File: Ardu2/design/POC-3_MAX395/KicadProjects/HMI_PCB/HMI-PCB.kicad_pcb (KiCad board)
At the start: 2 copper layers, 170.2 x 75.2 mm, 41 parts, among them P1 SplitPot_0_M, P10 TREM_VIB, P11 SplitPot_5_TR, P12 Analog Power IN, P13 Digital Power IN/OUT, P2 SEQ_SAVE, P3 SplitPot_1_A, P4 SplitPot_2_B, P5 PB_OUT, P6 Analog_Out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

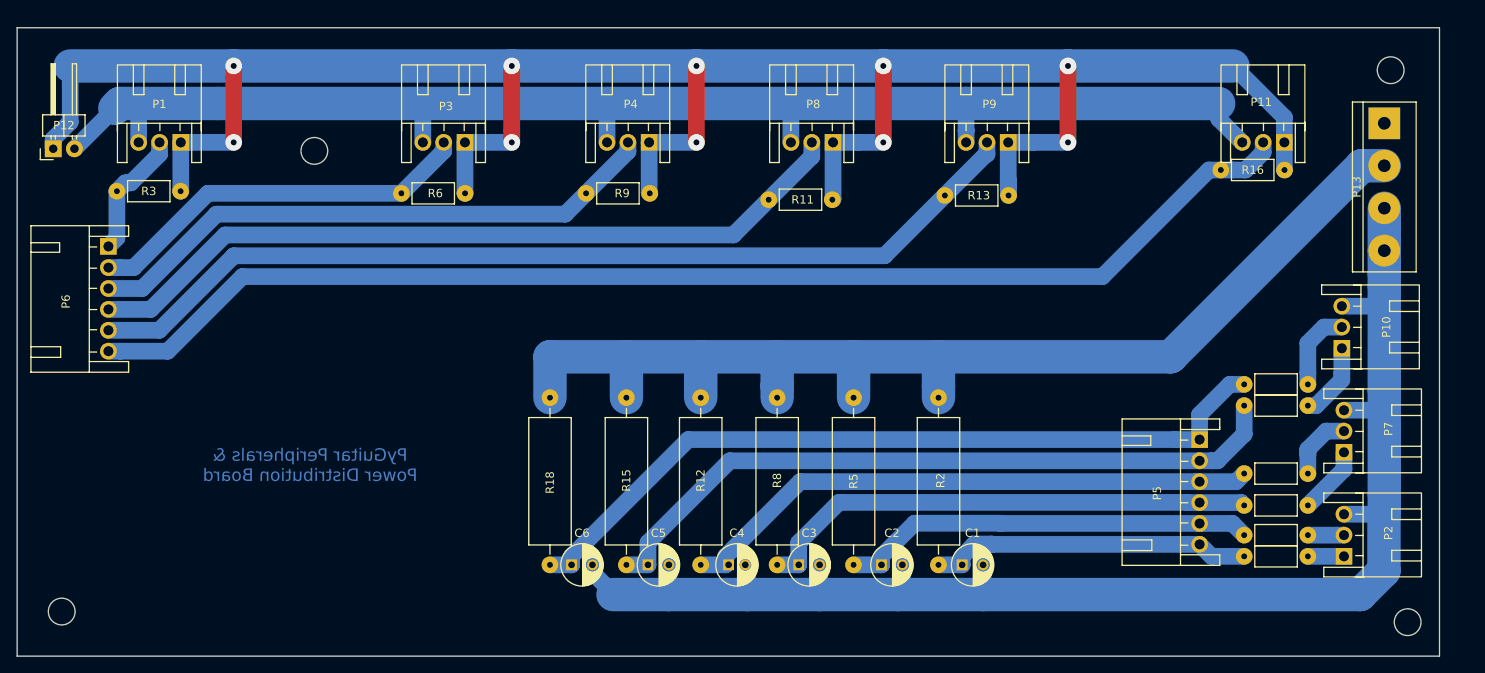
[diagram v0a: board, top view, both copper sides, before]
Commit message: updated peripherals PCB
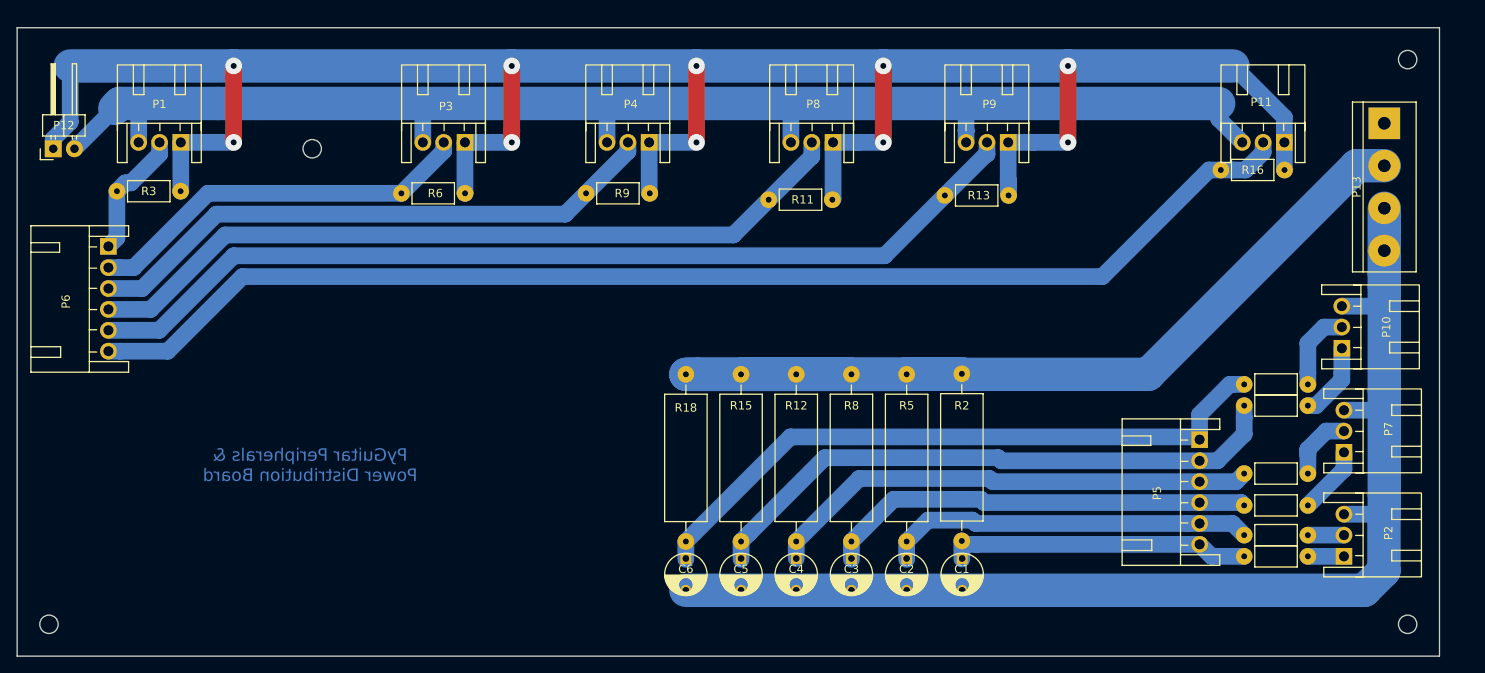
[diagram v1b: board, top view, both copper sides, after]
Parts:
- removed the REF** at (102.1, 86.9)
- removed the REF** at (232.9, 143.3)
- removed the REF** at (71.9, 142.0)
- removed the REF** at (230.9, 77.2)
- added REF**: MountingHole_2.2mm_M2, Mounting_Holes:MountingHole_2.2mm_M2, F.Cu at (70.4, 143.5)
- added REF**: MountingHole_2.2mm_M2, Mounting_Holes:MountingHole_2.2mm_M2, F.Cu at (101.9, 86.6)
- added REF**: MountingHole_2.2mm_M2, Mounting_Holes:MountingHole_2.2mm_M2, F.Cu at (232.9, 143.5)
- added REF**: MountingHole_2.2mm_M2, Mounting_Holes:MountingHole_2.2mm_M2, F.Cu at (232.9, 75.9)
- C1, C2, C3, C5, C6: footprint Capacitors_ThroughHole:C_Radial_D5_L11_P2.5 -> misc:C_Radial_D5_L11_P3.81
- C4: footprint Capacitors_ThroughHole:C_Radial_D5_L11_P2 -> misc:C_Radial_D5_L11_P3.81
- moved R18 16.5 mm to (146.6, 113.6)
- moved R15 14.0 mm to (153.2, 113.6)
- moved C6 13.7 mm to (146.6, 136.3), turned to 270 degrees
- moved R12 11.8 mm to (159.8, 113.6)
- moved C5 11.1 mm to (153.2, 136.3), turned to 270 degrees
- moved R8 9.32 mm to (166.4, 113.6)
- moved C4 8.10 mm to (159.8, 136.3), turned to 270 degrees
- moved R5 6.94 mm to (173.0, 113.6)
- moved C3 6.31 mm to (166.4, 136.3), turned to 270 degrees
- moved R2 4.00 mm to (179.6, 113.5)
- moved C2 3.01 mm to (173.0, 136.3), turned to 270 degrees
- moved C1 0.10 mm to (179.6, 136.3), turned to 270 degrees
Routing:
- net /GND_D: track 174.2 -> 142.7 mm
- net /X22: track 94.4 -> 78.8 mm
- net /X7: track 85.4 -> 71.4 mm
- net /Y6: track 70.2 -> 59.3 mm
- net /Y5: track 60.7 -> 51.5 mm
- net /Y4: track 50.0 -> 44.3 mm
- net /Y3: track 38.8 -> 36.7 mm
- net /3v3_D: track 138.6 -> 140.2 mm

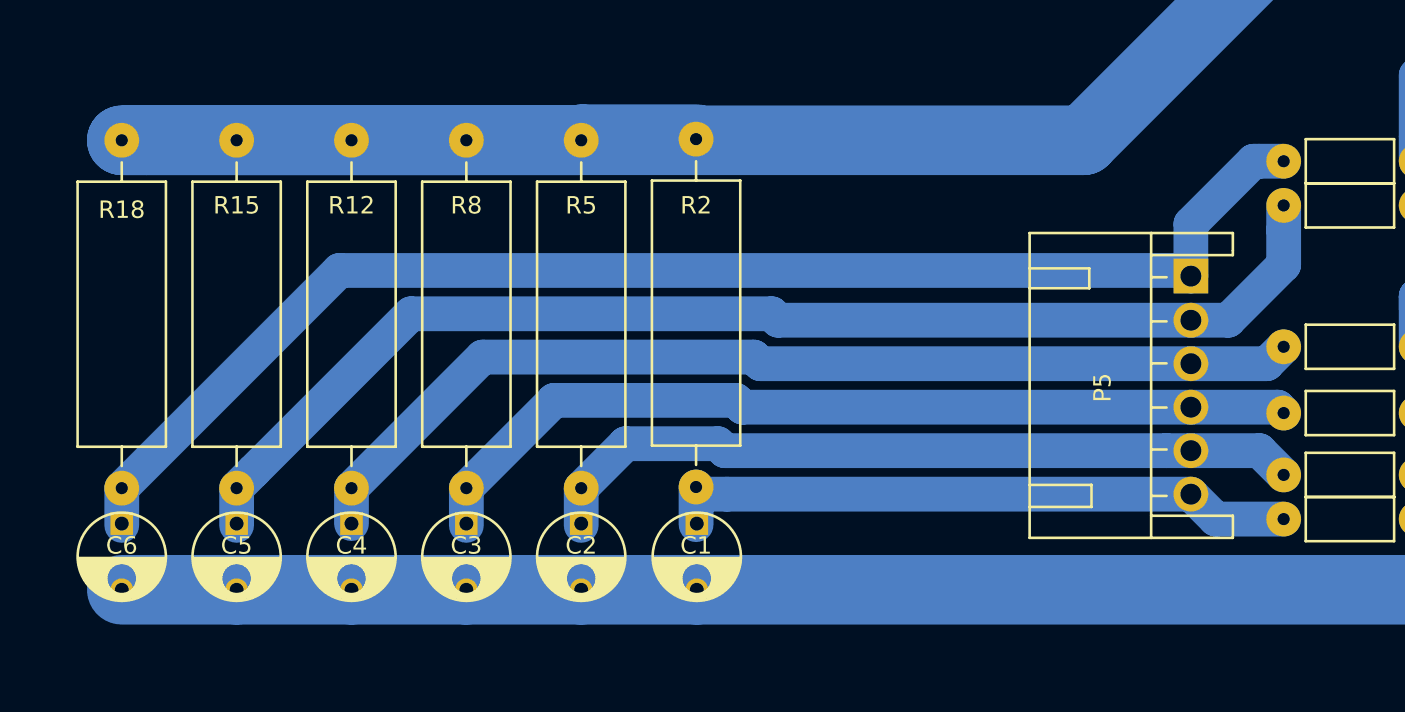
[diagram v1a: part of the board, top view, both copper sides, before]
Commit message: updated peripherals PCB
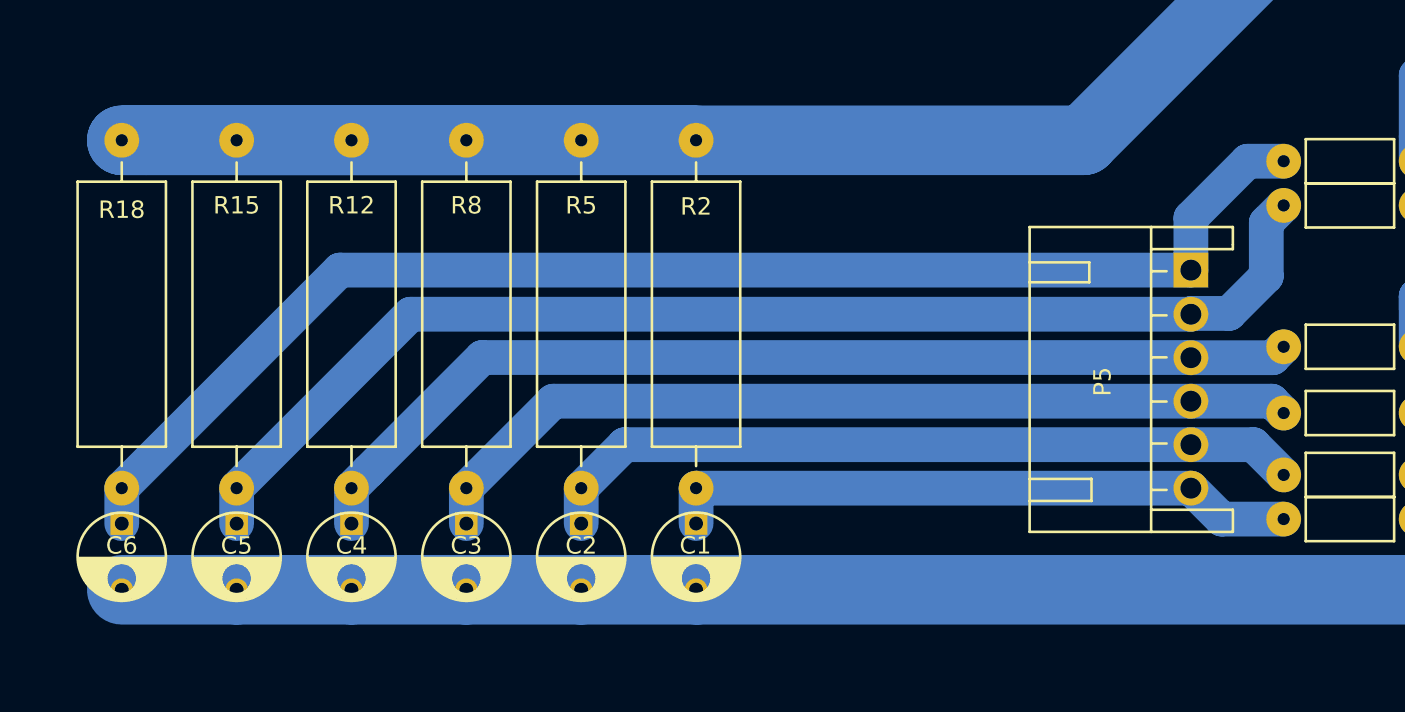
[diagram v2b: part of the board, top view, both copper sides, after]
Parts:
- moved P5 0.34 mm to (208.0, 121.1)
- moved R2 0.07 mm to (179.6, 113.6)
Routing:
- net /X7: track 71.4 -> 70.8 mm

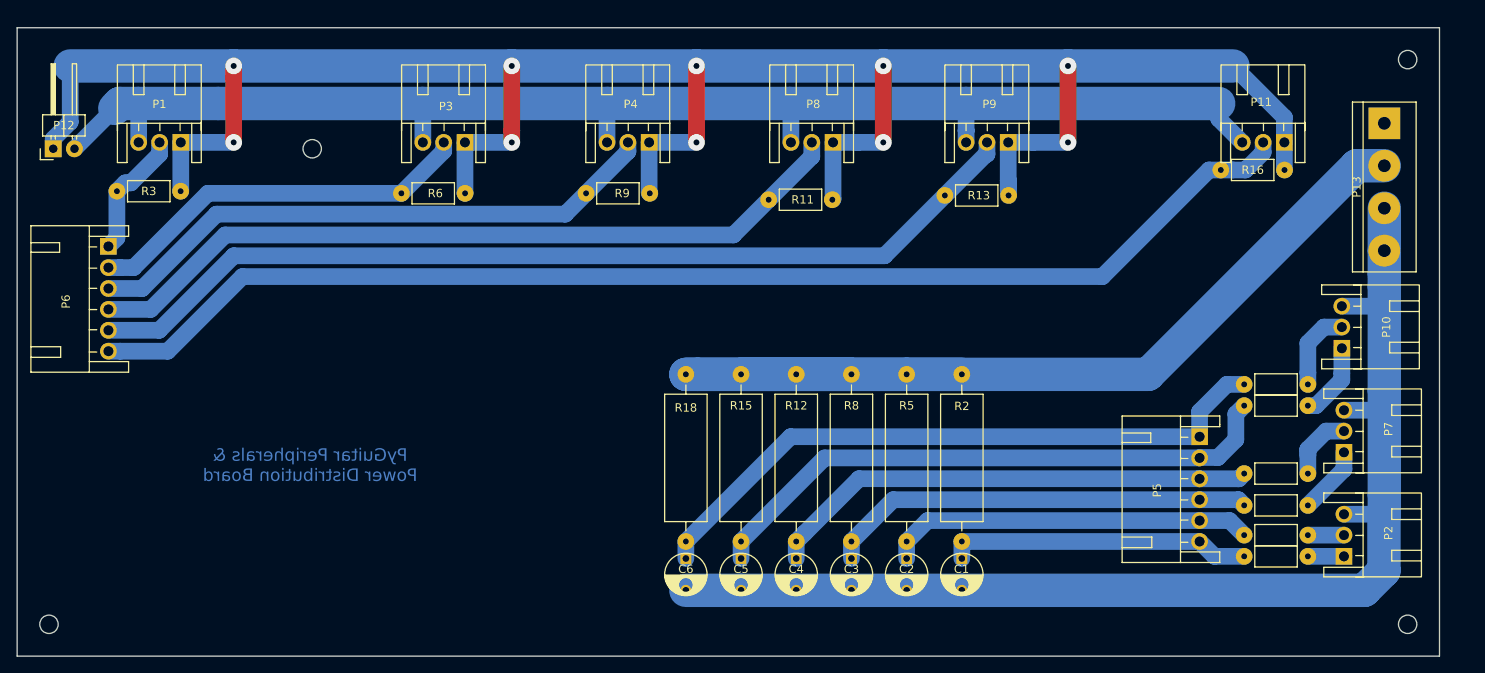
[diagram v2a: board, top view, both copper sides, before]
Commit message: updated peripherals PCB
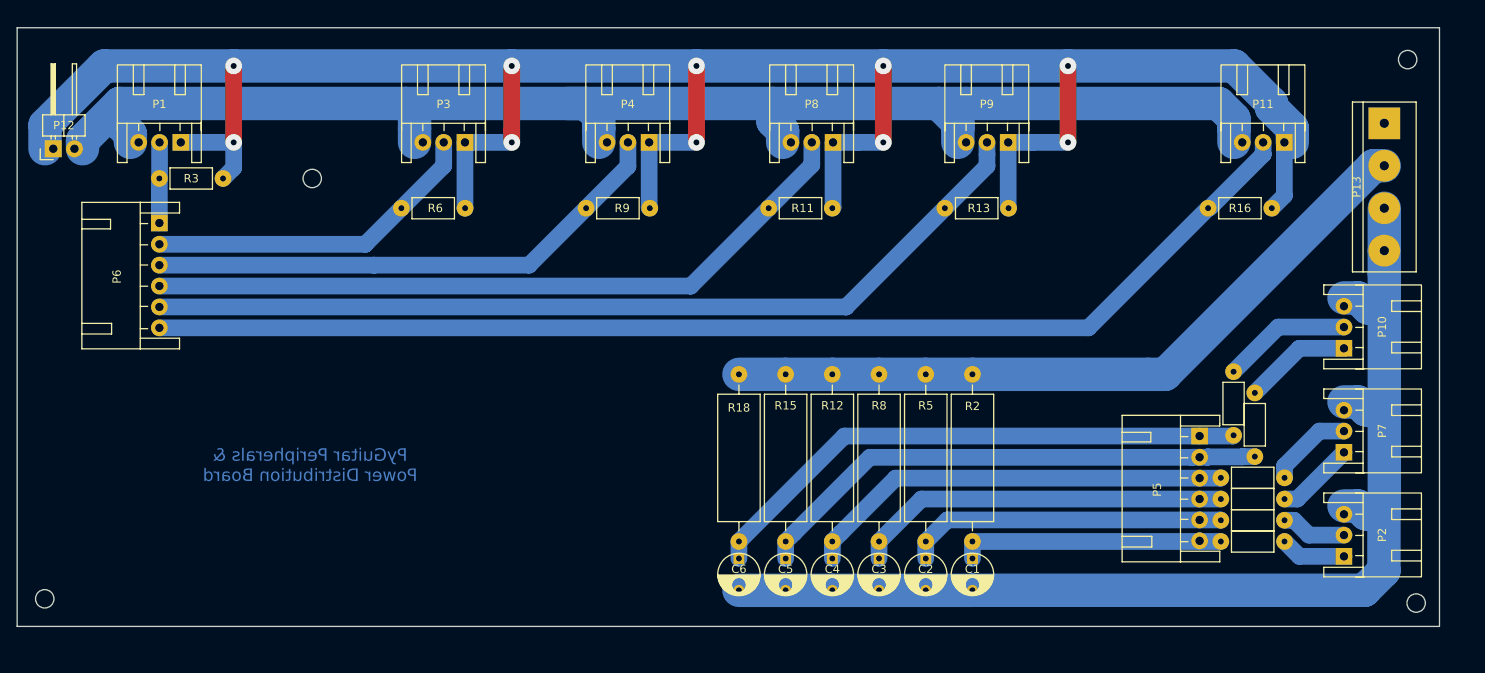
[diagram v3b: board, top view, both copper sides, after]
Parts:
- C1, C2, C3, C4, C5, C6: footprint misc:C_Radial_D5_L11_P3.81 -> misc:C_Radial_D5_L11_P3.81_0_7mm_Hole
- P1, P10, P11, P2, P3, P4, P7, P8, P9: footprint Connect:Wafer_Horizontal10x5.8x7RM2.5-3 -> misc:Wafer_Horizontal10x5.8x7RM2.5-3_1mmHole
- P12: footprint Pin_Headers:Pin_Header_Angled_1x02 -> misc:Pin_Header_Angled_1x02_1mm_hole
- P13: footprint Connect:bornier4 -> misc:bornier4_Dinkle
- P5, P6: footprint Connect:Wafer_Horizontal17.5x5.8x7RM2.5-6 -> misc:Wafer_Horizontal17.5x5.8x7RM2.5-6_1mm_Hole
- moved P6 6.71 mm to (83.6, 95.5)
- moved C6 6.35 mm to (152.9, 136.3)
- moved R18 6.35 mm to (152.9, 113.6)
- moved R14 6.23 mm to (214.6, 123.4), turned to 90 degrees
- moved R17 6.23 mm to (212.1, 120.9), turned to 90 degrees
- moved C5 5.33 mm to (158.5, 136.3)
- moved R15 5.33 mm to (158.5, 113.6)
- moved R3 5.30 mm to (83.6, 90.2)
- moved R16 4.82 mm to (209.0, 93.7)
- moved C4 4.32 mm to (164.1, 136.3)
- moved R12 4.32 mm to (164.1, 113.6)
- moved REF** 3.56 mm to (101.9, 90.2)
- moved R4 3.31 mm to (210.6, 131.1)
- moved R1 3.31 mm to (210.6, 133.6)
- moved C3 3.30 mm to (169.7, 136.3)
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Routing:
- net /3v3_D: track 140.1 -> 87.6 mm
- net /X22: track 78.4 -> 66.5 mm
- net /X7: track 70.8 -> 62.4 mm
- net /GND_A: track 274.0 -> 281.5 mm
- net /Y6: track 59.0 -> 51.7 mm
- net /Y12: track 149.2 -> 141.9 mm
- net /X4: track 93.4 -> 86.8 mm
- net /Y11: track 115.3 -> 108.8 mm
- net /Y5: track 51.4 -> 45.0 mm
- net /X3: track 70.0 -> 63.8 mm
- net /X2: track 46.9 -> 40.7 mm
- net /Y4: track 44.2 -> 38.4 mm
- net /X1: track 15.4 -> 9.66 mm
- net /PB_3: track 9.80 -> 15.4 mm
- net /GND_D: track 142.7 -> 137.5 mm
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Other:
- board size 170.2 x 75.2 mm -> 170.2 x 71.6 mm
- rule trace_min: 0.2 -> 2
- rule via_min_size: 0.4 -> 2
